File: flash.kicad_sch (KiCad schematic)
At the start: 0 parts

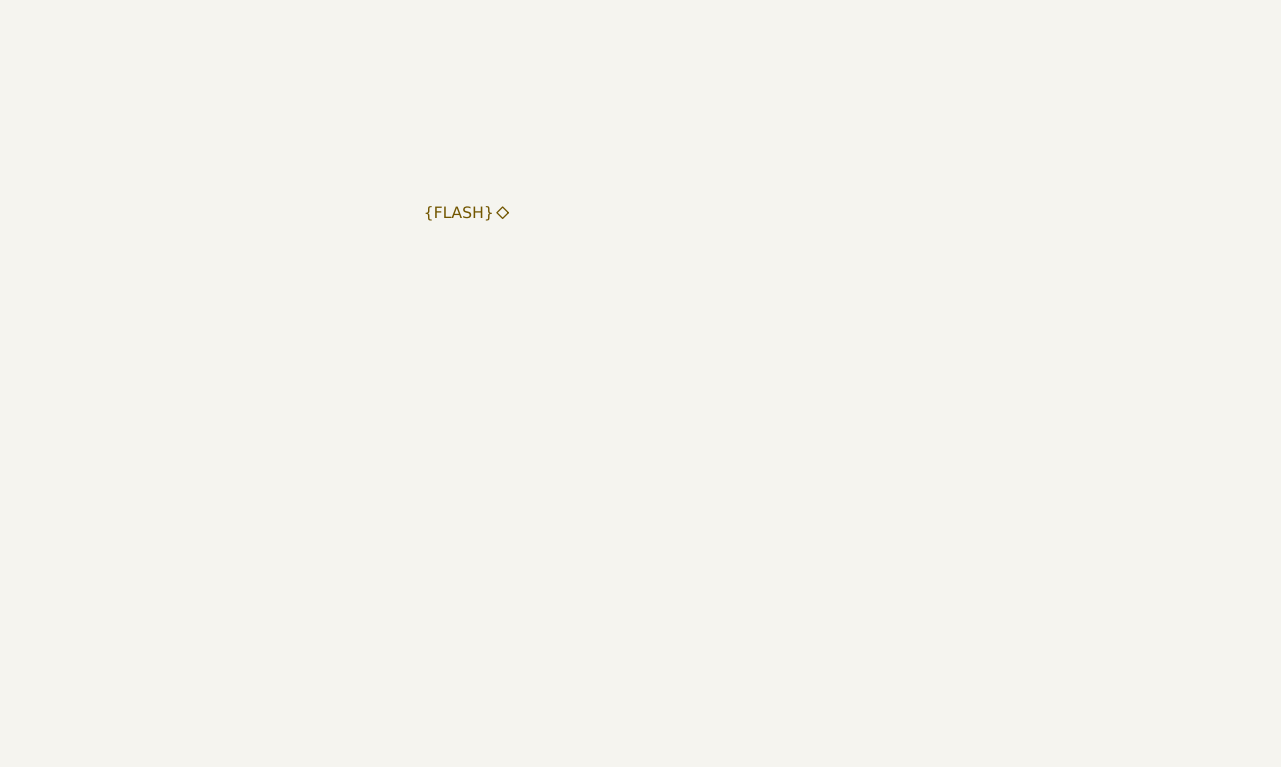
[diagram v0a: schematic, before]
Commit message: Nand Flash, Sata Connectors and removing (hopefully) unnecessary things
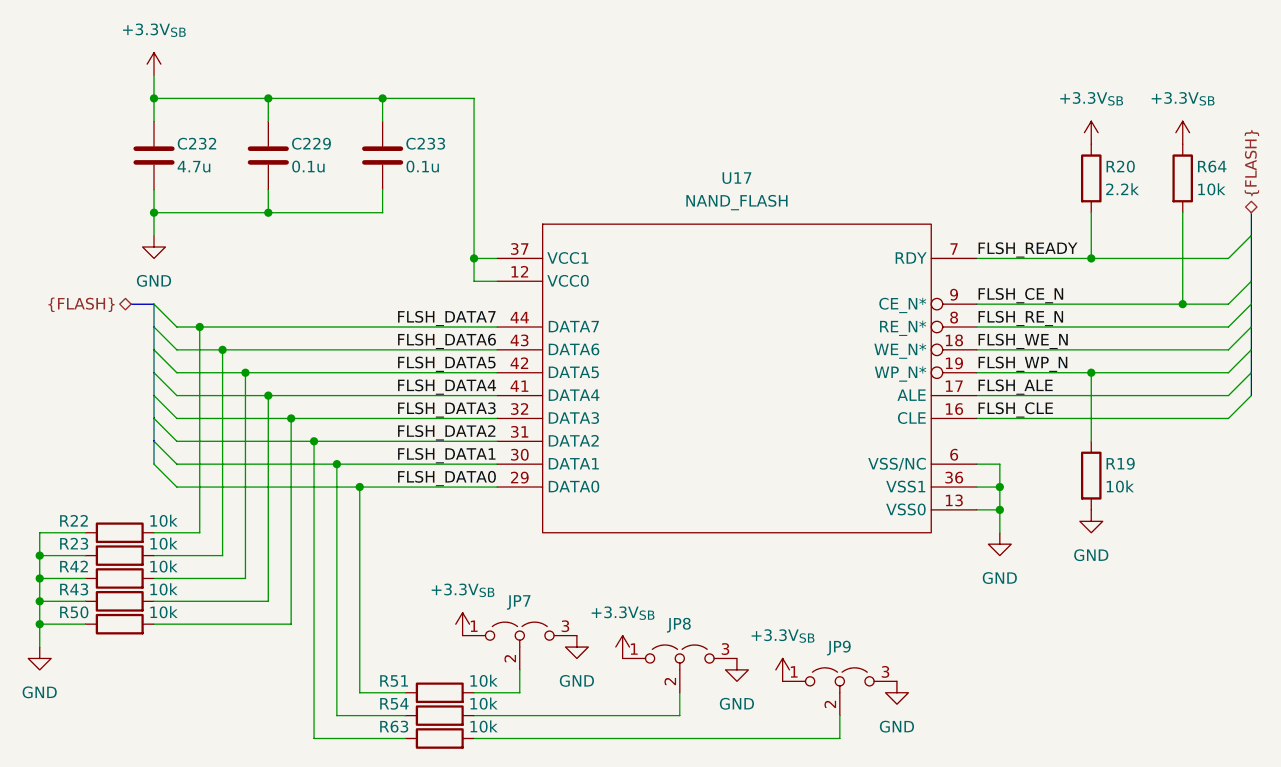
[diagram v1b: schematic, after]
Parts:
- added C229, C233: 0.1u, symbol Device:C
- added C232: 4.7u, symbol Device:C
- added JP7, JP8, JP9: Jumper_3_Open, symbol Jumper:Jumper_3_Open
- added R19, R22, R23, R42, R43, R50, R51, R54, R63, R64: 10k, symbol Device:R
- added R20: 2.2k, symbol Device:R
- added U17: NAND_FLASH, symbol FLASH:NAND_FLASH
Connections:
- new net: JP8.2 (C), R54.2
- new net: U17.1 (NC0), U17.10 (NC5), U17.11 (NC6), U17.14 (NC7), U17.15 (NC8), U17.2 (NC1), U17.20 (NC9), U17.21 (NC10), U17.22 (NC11), U17.23 (NC12), U17.24 (NC13), U17.25 (NC14), U17.26 (NC15), U17.27 (NC16), U17.28 (NC17), U17.3 (NC2), U17.33 (NC18), U17.34 (NC19), U17.35 (NC20), U17.38 (NC27), U17.39 (NC21), U17.4 (NC3), U17.40 (NC22), U17.45 (NC23), U17.46 (NC24), U17.47 (NC25), U17.48 (NC26), U17.5 (NC4)
- new net: JP9.2 (C), R63.2
- new net: JP7.2 (C), R51.2
- new net +3.3V_{SB}: C229.1, C232.1, C233.1, JP7.1 (A), JP8.1 (A), JP9.1 (A), R20.1, R64.1, U17.12 (VCC0), U17.37 (VCC1)
- new net FLSH_ALE: U17.17 (ALE)
- new net FLSH_CE_N: R64.2, U17.9 (CE_N*)
- new net FLSH_CLE: U17.16 (CLE)
- new net FLSH_DATA0: R51.1, U17.29 (DATA0)
- new net FLSH_DATA1: R54.1, U17.30 (DATA1)
- new net FLSH_DATA2: R63.1, U17.31 (DATA2)
- new net FLSH_DATA3: R50.2, U17.32 (DATA3)
- new net FLSH_DATA4: R43.2, U17.41 (DATA4)
- new net FLSH_DATA5: R42.2, U17.42 (DATA5)
- new net FLSH_DATA6: R23.2, U17.43 (DATA6)
- new net FLSH_DATA7: R22.2, U17.44 (DATA7)
- new net FLSH_READY: R20.2, U17.7 (RDY)
- new net FLSH_RE_N: U17.8 (RE_N*)
- new net FLSH_WE_N: U17.18 (WE_N*)
- new net FLSH_WP_N: R19.1, U17.19 (WP_N*)
- new net GND: C229.2, C232.2, C233.2, JP7.3 (B), JP8.3 (B), JP9.3 (B), R19.2, R22.1, R23.1, R42.1, R43.1, R50.1, U17.13 (VSS0), U17.36 (VSS1), U17.6 (VSS/NC)

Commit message: Multipurpose and standby power rails, Reannotated schematic
Added V_1P2, V_1P8, V_5P0DUAL, V_EFUSE, V_GPUPCIE, V_3P3STBY and V_1P2STBY
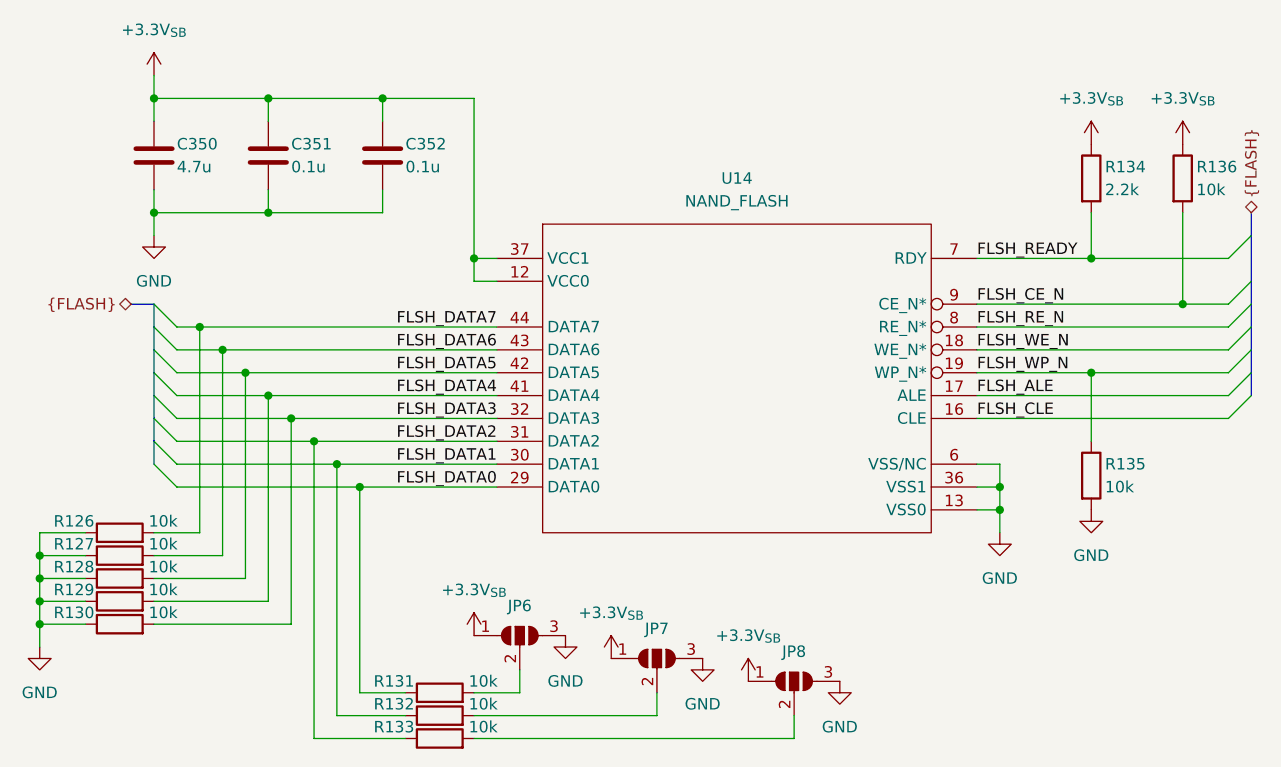
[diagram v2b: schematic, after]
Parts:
- removed JP7, JP8, JP9: Jumper_3_Open, symbol Jumper:Jumper_3_Open
- added JP6, JP7, JP8: SolderJumper_3_Open, symbol Jumper:SolderJumper_3_Open
- renumbered C232 to C350, C229 to C351, C233 to C352, R22 to R126, R23 to R127, R42 to R128, R43 to R129, R50 to R130, R51 to R131, R54 to R132, R63 to R133, R20 to R134, R19 to R135, R64 to R136, U17 to U14
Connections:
- net +3.3V_{SB}: now also JP6.1 (A), JP7.1 (A), JP8.1 (A)
- net GND: now also JP6.3 (B), JP7.3 (B), JP8.3 (B)
- net at R132.2: now also JP7.2 (C)
- net at R133.2: now also JP8.2 (C)
- net at R131.2: now also JP6.2 (C)
